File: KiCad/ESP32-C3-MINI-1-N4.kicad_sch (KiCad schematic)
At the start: 0 parts

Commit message: Add ESP32-C3-Mini
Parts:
- added C? (x4): 1u, Capacitor_SMD:C_0402_1005Metric_Pad0.74x0.62mm_HandSolder, symbol Device:C
- added CR? (x2): CUS08F30_H3FT, CUS08F30:USC_TOS, symbol 2023-10-06_10-19-56:CUS08F30_H3FT
- added D?: Green, LED_SMD:LED_0201_0603Metric_Pad0.64x0.40mm_HandSolder, symbol Device:LED
- added D?: Red, LED_SMD:LED_0201_0603Metric_Pad0.64x0.40mm_HandSolder, symbol Device:LED
- added JP? (x2): Jumper_2_Open, symbol Jumper:Jumper_2_Open
- added R? (x4): 1k, Resistor_SMD:R_0402_1005Metric_Pad0.72x0.64mm_HandSolder, symbol Device:R
- added R? (x4): 10.5k, Resistor_SMD:R_0402_1005Metric_Pad0.72x0.64mm_HandSolder, symbol Device:R
- added TP?: ~, symbol 2023-09-11_18-18-06:TC2030
- added U?: ESP32-C3-MINI-1-N4, ESP32-C3-MINI-1_EXP, symbol 2023-09-11_18-18-06:ESP32-C3-MINI-1-N4
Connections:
- new net: JP?.1 (A), R?.2 (x2)
- new net: D?.2 (A), R?.2 (x2)
- new net: C?.1, CR?.1, R?.1
- new net: C?.1, R?.2, U?.8 (EN)
- new net +3.3V: C?.1, R?.1, R?.1, R?.1, R?.1, R?.1, R?.1, U?.3 (3V3)
- new net +5V-Prog: TP?.2
- new net ESP-Boot: CR?.1, TP?.6
- new net ESP-En: TP?.1
- new net ESP-Rx: TP?.5, U?.30 (RXD0)
- new net ESP-Tx: TP?.3, U?.31 (TXD0)
- new net GND: C?.2, C?.2, C?.2, C?.2, D?.1 (K), JP?.2 (B), JP?.2 (B), TP?.4, U?.1 (GND), U?.11 (GND), U?.14 (GND), U?.2 (GND), U?.36 (GND), U?.37 (GND), U?.38 (GND), U?.39 (GND), U?.40 (GND), U?.41 (GND), U?.42 (GND), U?.43 (GND), U?.44 (GND), U?.45 (GND), U?.46 (GND), U?.47 (GND), U?.48 (GND), U?.49 (GND), U?.50 (GND), U?.51 (GND), U?.52 (GND), U?.53 (GND), U?.54 (GND), U?.55 (GND), U?.56 (GND), U?.57 (GND), U?.58 (GND), U?.59 (GND), U?.60 (GND), U?.61 (GND)
- new net Input-Boot: CR?.2, CR?.2, R?.2, U?.12 (IO0), U?.5 (IO2)
- new net Input-Reset: C?.1, R?.1, R?.2
- new net User-LED: D?.1 (K), R?.2, U?.22 (IO8)
- no-connect marks 0 -> 14
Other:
- note added: "LEDs"
- note added: "Programming Connector"
- note added: "User Input Jumpers"
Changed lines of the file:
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@@
 (kicad_sch (version 20230121) (generator eeschema)
   (paper "A4")
-)

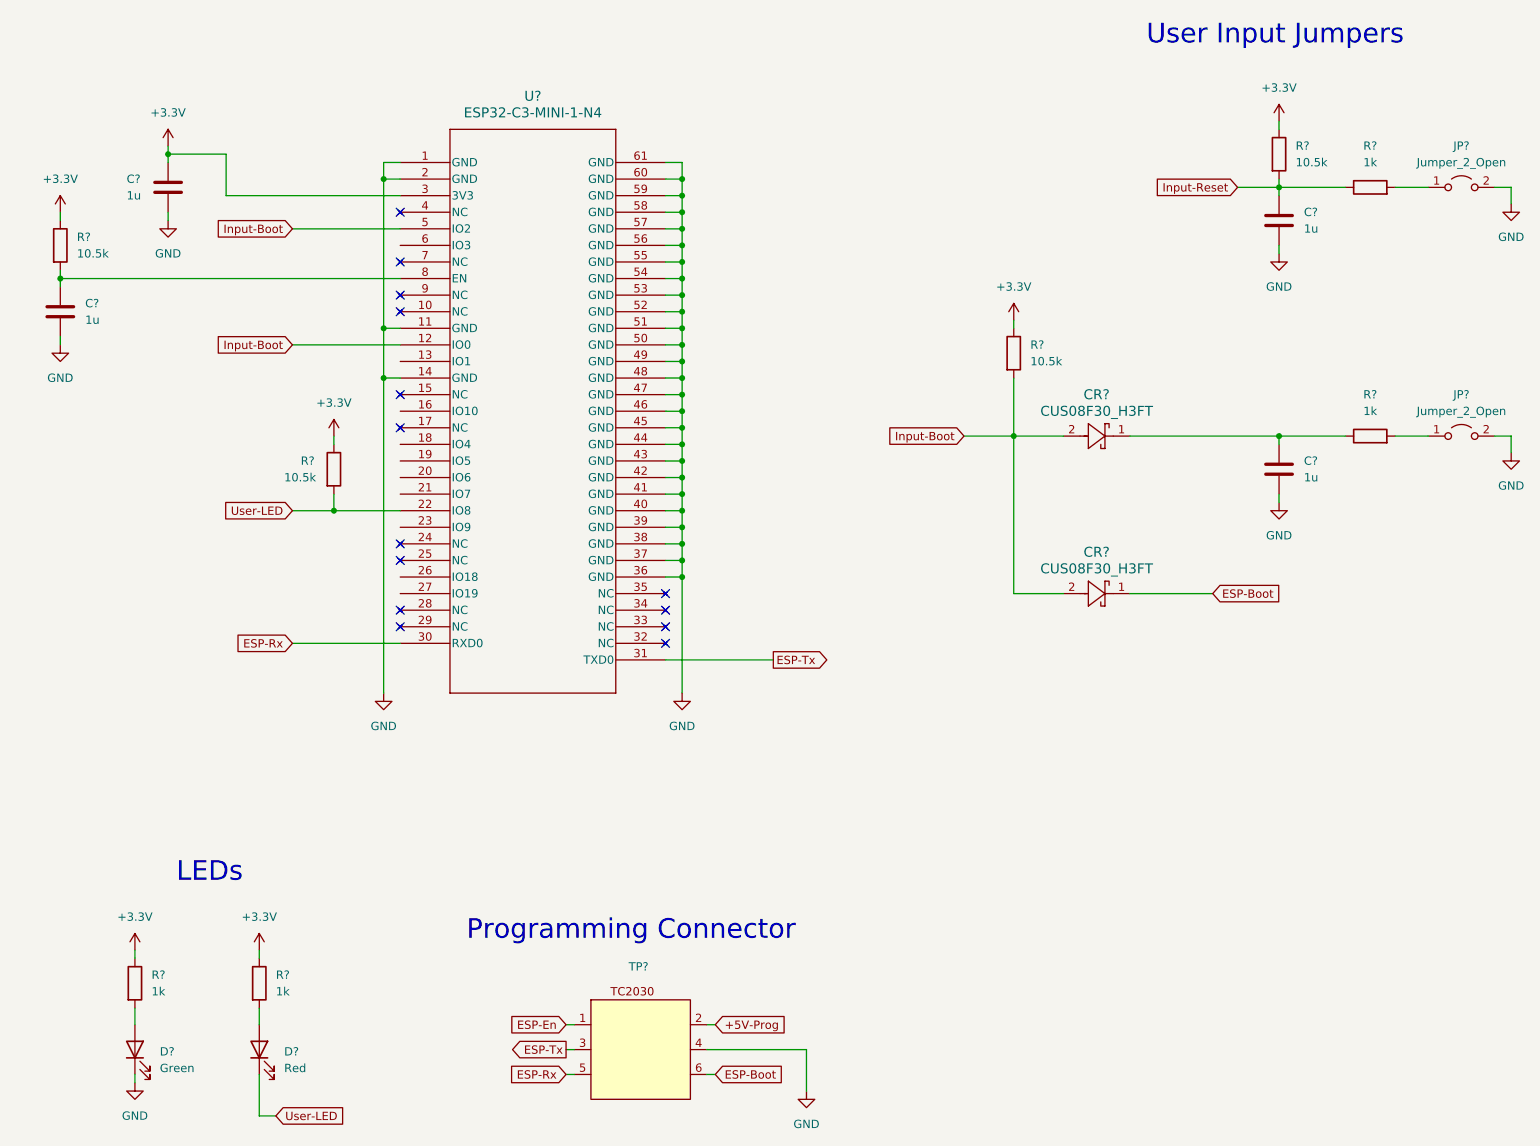
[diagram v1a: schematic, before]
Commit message: Add level shifters
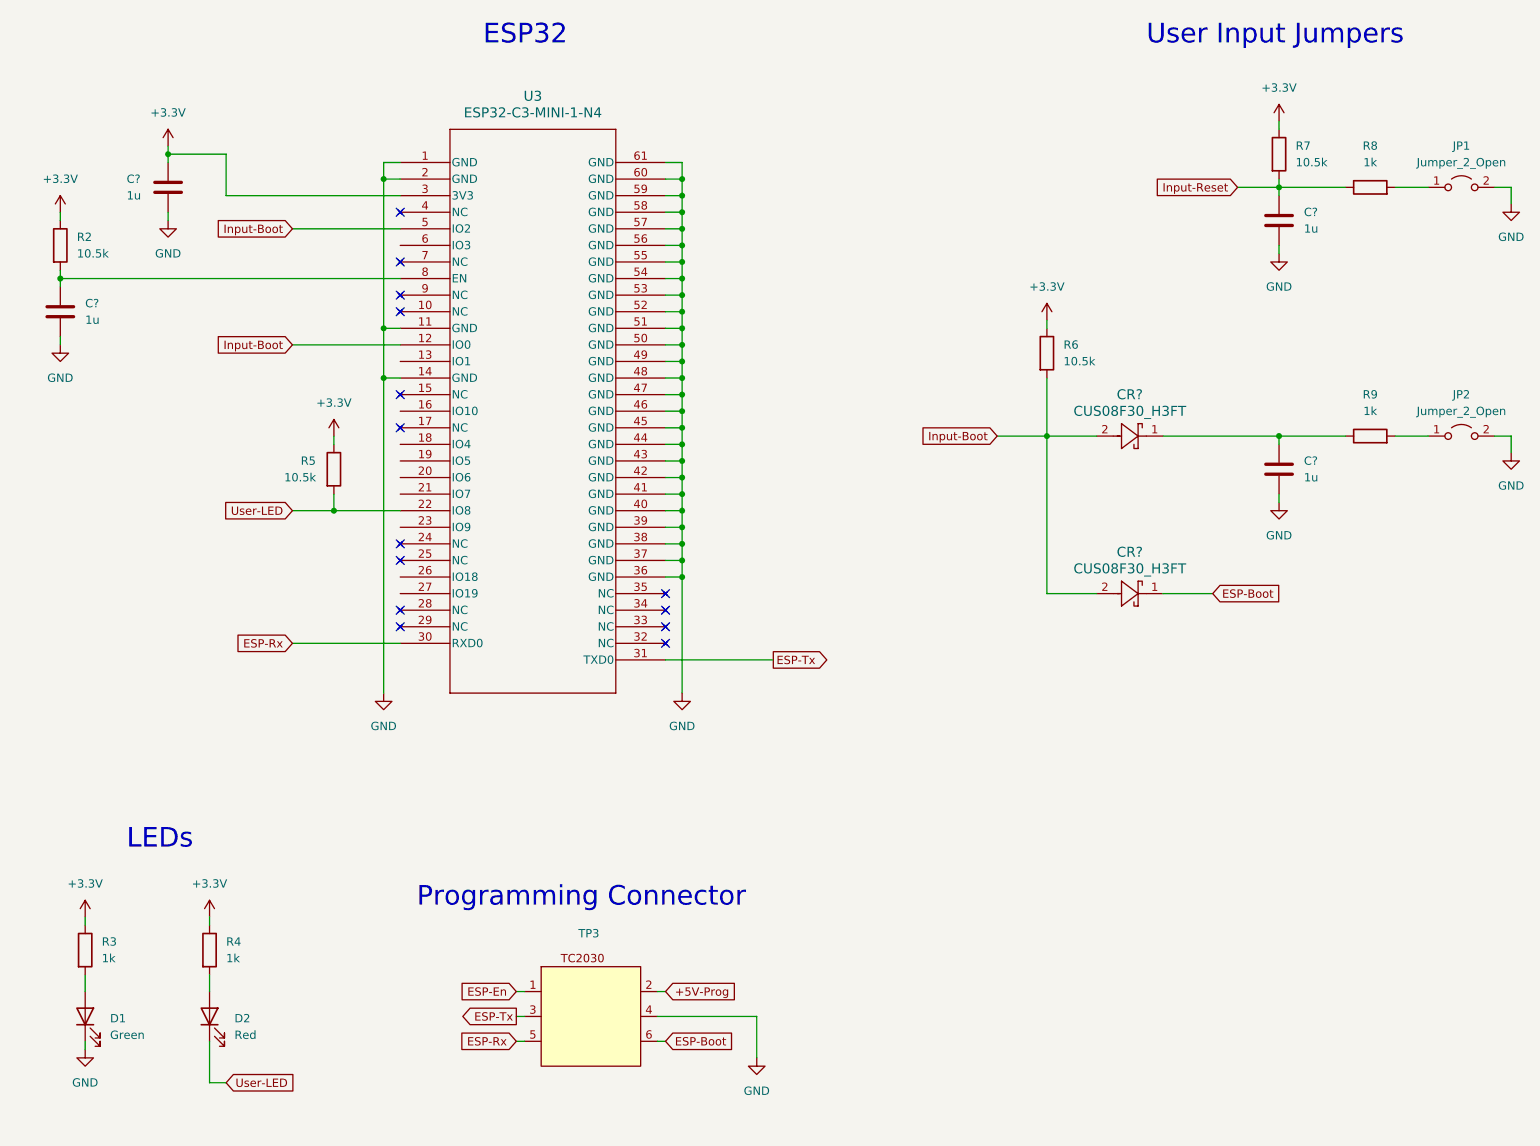
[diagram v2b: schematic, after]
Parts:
- gave numbers to parts that had none: 14
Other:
- note added: "ESP32"
- moved on the sheet: CR?, D1, D2, R3, R4, R6, TP3

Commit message: Change resistor values
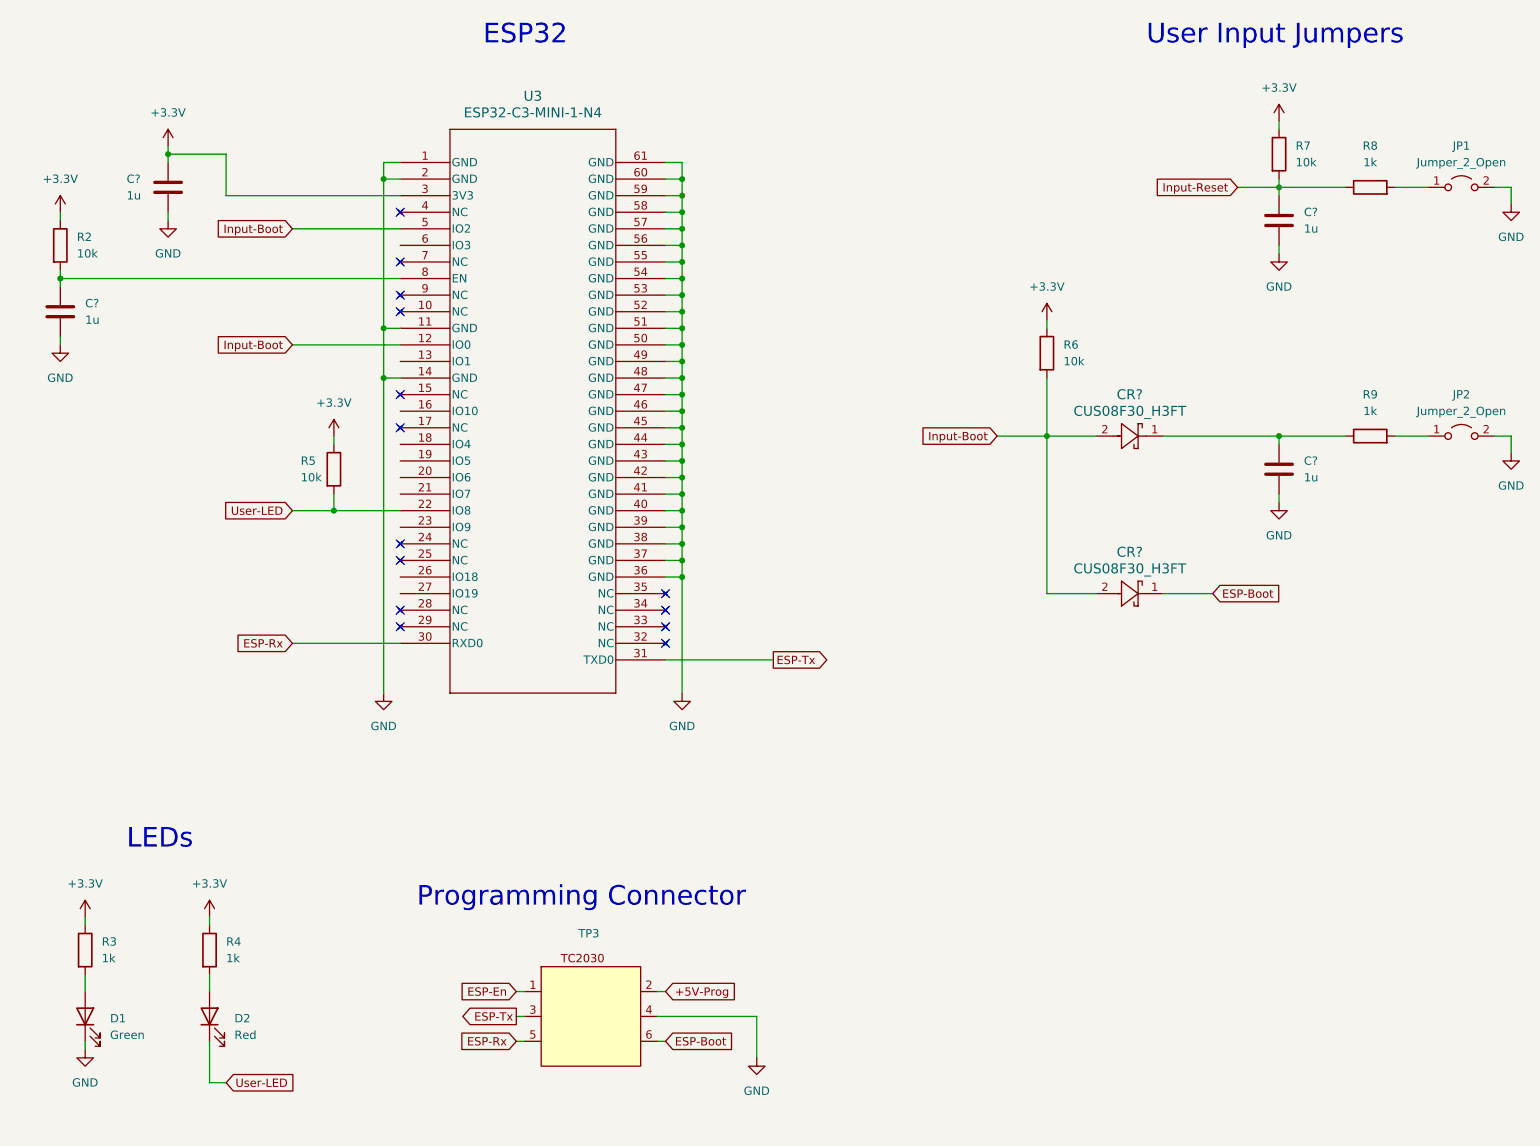
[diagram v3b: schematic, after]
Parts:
- R2, R5, R6, R7: value 10.5k -> 10k
- TP3: footprint (none) -> Connector:Tag-Connect_TC2030-IDC-NL_2x03_P1.27mm_Vertical

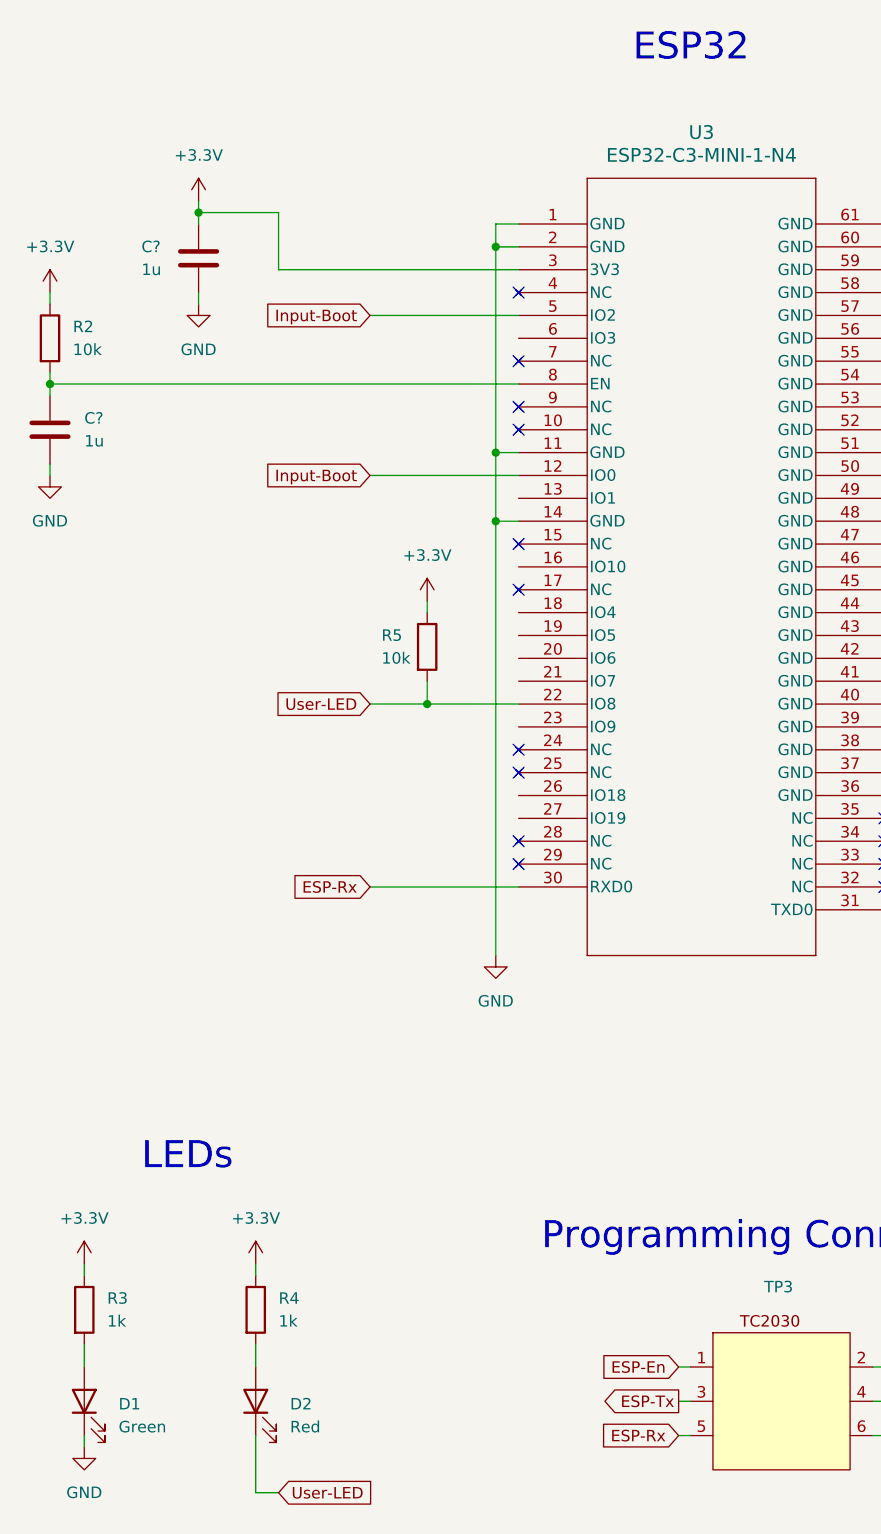
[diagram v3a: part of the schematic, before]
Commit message: Change reverse polarity protection, start the PCB design
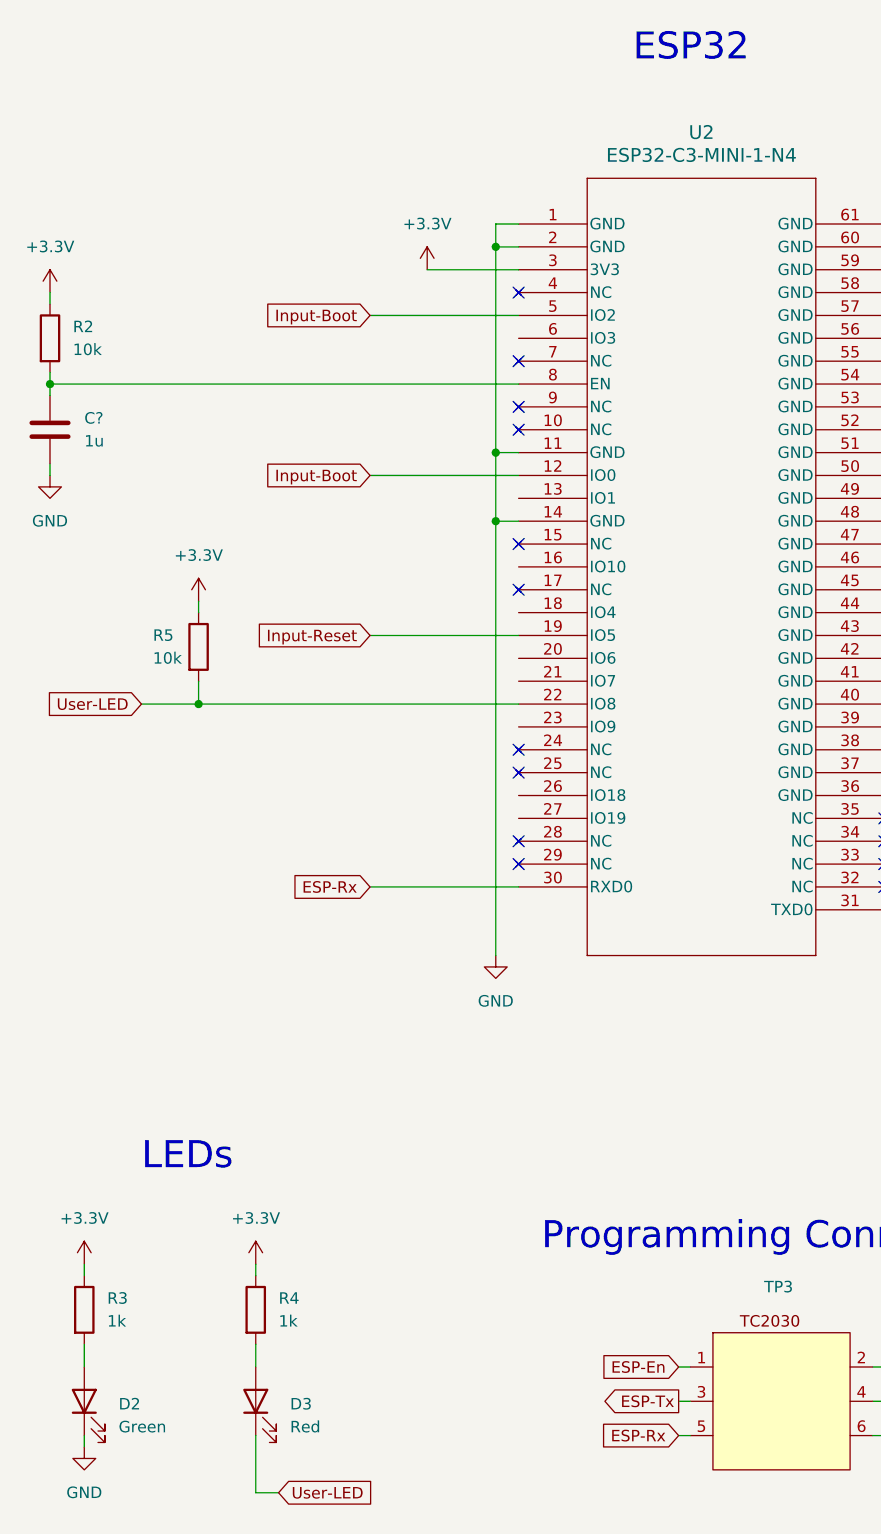
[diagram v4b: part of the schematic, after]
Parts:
- removed C?: 1u, Capacitor_SMD:C_0402_1005Metric_Pad0.74x0.62mm_HandSolder, symbol Device:C
- JP1, JP2: footprint (none) -> Jumper:SolderJumper-2_P1.3mm_Open_RoundedPad1.0x1.5mm
- U2: renamed from U3; footprint ESP32-C3-MINI-1_EXP -> ESP32-C3-MINI-1-N4:ESP32-C3-MINI-1_EXP
- renumbered D1 to D2, D2 to D3
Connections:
- net Input-Reset: now also U2.19 (IO5)
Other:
- moved on the sheet: R5
